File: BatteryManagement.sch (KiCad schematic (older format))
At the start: 0 parts

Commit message: Starting battery protection & management.
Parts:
- added U?: AP9211, symbol dingo-hat:AP9211
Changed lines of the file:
@@
 $Descr A4 11693 8268
 encoding utf-8
-Sheet 1 3
+Sheet 3 3
 Title ""
 Date ""
@@
 Comment4 ""
 $EndDescr
+$Comp
+L dingo-hat:AP9211 U?
+U 1 1 5DC173E3
+P 4400 3500
+F 0 "U?" H 4400 3925 50  0000 C CNN
+F 1 "AP9211" H 4400 3834 50  0000 C CNN
+F 2 "" H 4400 3350 50  0001 C CNN
+F 3 "https://www.diodes.com/assets/Datasheets/AP9211.pdf" H 4400 3350 50  0001 C CNN
+	1    4400 3500
+	1    0    0    -1
+$EndComp
 $EndSCHEMATC

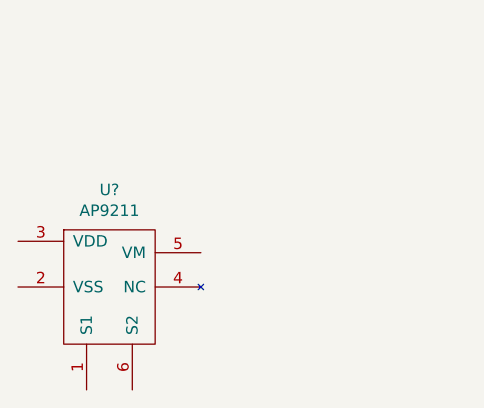
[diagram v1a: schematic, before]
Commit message: Changing structure, RM old power circuitry.
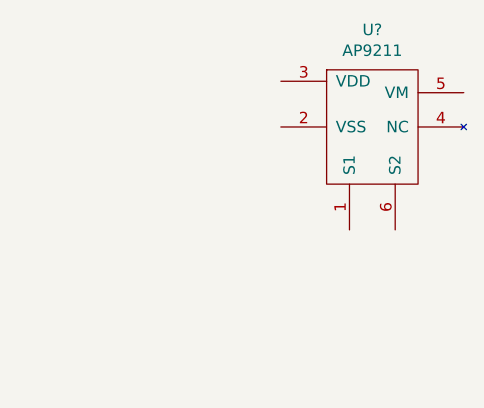
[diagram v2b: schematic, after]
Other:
- moved on the sheet: U?
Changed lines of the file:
@@
 L dingo-hat:AP9211 U?
 U 1 1 5DC173E3
-P 4400 3500
-F 0 "U?" H 4400 3925 50  0000 C CNN
-F 1 "AP9211" H 4400 3834 50  0000 C CNN
-F 2 "" H 4400 3350 50  0001 C CNN
-F 3 "https://www.diodes.com/assets/Datasheets/AP9211.pdf" H 4400 3350 50  0001 C CNN
-	1    4400 3500
+P 5550 2800
+AR Path="/5DA95EB0/5DAAD200/5DC173E3" Ref="U?"  Part="1"
+AR Path="/5DC297AB/5DC173E3" Ref="U?"  Part="1"
+F 0 "U?" H 5550 3225 50  0000 C CNN
+F 1 "AP9211" H 5550 3134 50  0000 C CNN
+F 2 "" H 5550 2650 50  0001 C CNN
+F 3 "https://www.diodes.com/assets/Datasheets/AP9211.pdf" H 5550 2650 50  0001 C CNN
+	1    5550 2800
 	1    0    0    -1
 $EndComp

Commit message: Battery work, need to get on to connectors.
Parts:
- added C401: 100nF, Capacitors_SMD:C_0603, symbol Device:C
- added J401: Bootstrap, Pin_Headers:Pin_Header_Straight_1x02_Pitch2.54mm, symbol Connector_Generic:Conn_01x02
- added R401: 470, Resistor_SMD:R_0603_1608Metric_Pad1.05x0.95mm_HandSolder, symbol Device:R
- added R402: 2k7, Resistor_SMD:R_0603_1608Metric_Pad1.05x0.95mm_HandSolder, symbol Device:R
- gave numbers to parts that had none: 1
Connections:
- net Batt-: now reaches U401.1 (S1)
- net Batt-: now also U401.2 (VSS), C401.2, J401.2 (Pin_2)
- net at U401.3 (VDD): now also C401.1, R401.2
- net BATT_S1: now reaches U401.5 (VM)
- net BATT_S1: now also R402.1
- net Pack-: now reaches U401.6 (S2)
- net Pack-: now also J401.1 (Pin_1), R402.2
- new net Batt+: R401.1
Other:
- note added: "Not sure if we'll need this to bring battery up on connect. Just do TH to check."
- moved on the sheet: U401
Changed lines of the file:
@@
 L dingo-hat:AP9211 U?
 U 1 1 5DC173E3
-P 5550 2800
+P 5550 3000
 AR Path="/5DA95EB0/5DAAD200/5DC173E3" Ref="U?"  Part="1"
-AR Path="/5DC297AB/5DC173E3" Ref="U?"  Part="1"
-F 0 "U?" H 5550 3225 50  0000 C CNN
-F 1 "AP9211" H 5550 3134 50  0000 C CNN
-F 2 "" H 5550 2650 50  0001 C CNN
-F 3 "https://www.diodes.com/assets/Datasheets/AP9211.pdf" H 5550 2650 50  0001 C CNN
-	1    5550 2800
+AR Path="/5DC297AB/5DC173E3" Ref="U401"  Part="1"
+F 0 "U401" H 5550 3425 50  0000 C CNN
+F 1 "AP9211" H 5550 3334 50  0000 C CNN
+F 2 "" H 5550 2850 50  0001 C CNN
+F 3 "https://www.diodes.com/assets/Datasheets/AP9211.pdf" H 5550 2850 50  0001 C CNN
+	1    5550 3000
 	1    0    0    -1
 $EndComp
+$Comp
+L Device:C C?
+U 1 1 5DD0667E
+P 4700 3050
+AR Path="/5DD0667E" Ref="C?"  Part="1"
+AR Path="/5DA95EB0/5DD0667E" Ref="C?"  Part="1"
+AR Path="/5DC297AB/5DD0667E" Ref="C401"  Part="1"
+F 0 "C401" H 4815 3096 50  0000 L CNN
+F 1 "100nF" H 4815 3005 50  0000 L CNN
+F 2 "Capacitors_SMD:C_0603" H 4738 2900 50  0001 C CNN
+F 3 "~" H 4700 3050 50  0001 C CNN
+F 4 "0603" H 4600 3150 50  0000 L TNN "Package"
+F 5 "CAP CER 0.1UF 50V X7R 0603" H 4700 3050 50  0001 C CNN "Description"
+F 6 "50V" H 4700 3000 50  0000 R TNN "Voltage Rating"
+F 7 "https://www.digikey.com/product-detail/en/samsung-electro-mechanics/CL10B104KB8NNNC/1276-1000-1-ND/3889086" H 4700 3050 50  0001 C CNN "Link"
+F 8 "Digi-Key" H 4700 3050 50  0001 C CNN "Supplier 1"
+F 9 "1276-1000-1-ND" H 4700 3050 50  0001 C CNN "Supplier Part Number 1"
+F 10 "0.15000" H 4700 3050 50  0001 C CNN "Unit Cost A$"
+	1    4700 3050
+	1    0    0    -1
+$EndComp
+$Comp
+L Device:R R?
+U 1 1 5DE42ED8
+P 6450 3150
+AR Path="/5DE42ED8" Ref="R?"  Part="1"
+AR Path="/5DC297AB/5DE42ED8" Ref="R402"  Part="1"
+F 0 "R402" V 6350 3050 50  0000 C CNN
+F 1 "2k7" V 6350 3250 50  0000 C CNN
+F 2 "Resistor_SMD:R_0603_1608Metric_Pad1.05x0.95mm_HandSolder" V 6380 3150 50  0001 C CNN
+F 3 "~" H 6450 3150 50  0001 C CNN
+F 4 "0603" H 5150 -2900 50  0001 C CNN "Package"
+	1    6450 3150
+	1    0    0    -1
+$EndComp
+Wire Wire Line
+	7450 3550 6450 3550
+Wire Wire Line
+	6450 3000 6450 2850
+Wire Wire Line
+	6450 2850 5950 2850
+Wire Wire Line
+	4700 2200 4700 2400
+Wire Wire Line
+	4700 2700 4700 2800
+Wire Wire Line
+	5450 3450 5450 3550
+Wire Wire Line
+	5450 3550 5100 3550
+Wire Wire Line
+	4700 3550 4700 3200
+Wire Wire Line
+	4700 2900 4700 2800
+Connection ~ 4700 2800
+Wire Wire Line
+	5150 3000 5100 3000
+Wire Wire Line
+	5100 3000 5100 3550
+Wire Wire Line
+	4700 3550 5100 3550
+Connection ~ 5100 3550
+Wire Wire Line
+	4700 2800 5150 2800
+Wire Wire Line
+	5650 3450 5650 3550
+Wire Wire Line
+	5650 3550 6450 3550
+Connection ~ 6450 3550
+Wire Wire Line
+	6450 3550 6450 3300
+Text HLabel 4700 2200 0    50   UnSpc ~ 0
+Batt+
+Text HLabel 7450 3550 2    50   UnSpc ~ 0
+Pack-
+Text HLabel 4700 3550 0    50   UnSpc ~ 0
+Batt-
+Wire Wire Line
+	4700 2200 7450 2200
+Text HLabel 7450 2200 2    50   UnSpc ~ 0
+Batt+
+$Comp
+L Device:R R?
+U 1 1 5DE426CE
+P 4700 2550
+AR Path="/5DE426CE" Ref="R?"  Part="1"
+AR Path="/5DC297AB/5DE426CE" Ref="R401"  Part="1"
+F 0 "R401" V 4600 2450 50  0000 C CNN
+F 1 "470" V 4600 2650 50  0000 C CNN
+F 2 "Resistor_SMD:R_0603_1608Metric_Pad1.05x0.95mm_HandSolder" V 4630 2550 50  0001 C CNN
+F 3 "~" H 4700 2550 50  0001 C CNN
+F 4 "0603" H 3400 -3500 50  0001 C CNN "Package"
+	1    4700 2550
+	1    0    0    -1
+$EndComp
+$Comp
+L Connector_Generic:Conn_01x02 J401
+U 1 1 5DE79FB0
+P 5600 3850
+F 0 "J401" V 5472 3930 50  0000 L CNN
+F 1 "Bootstrap" V 5563 3930 50  0000 L CNN
+F 2 "Pin_Headers:Pin_Header_Straight_1x02_Pitch2.54mm" H 5600 3850 50  0001 C CNN
+F 3 "~" H 5600 3850 50  0001 C CNN
+	1    5600 3850
+	0    1    1    0
+$EndComp
+Text Notes 5400 4000 0    50   ~ 0
+Not sure if we'll need this to bring battery up on connect. Just do TH to check.
+Wire Wire Line
+	5500 3650 5500 3550
+Wire Wire Line
+	5500 3550 5450 3550
+Connection ~ 5450 3550
+Wire Wire Line
+	5650 3550 5600 3550
+Wire Wire Line
+	5600 3550 5600 3650
+Connection ~ 5650 3550
+Text Label 6450 2850 0    50   ~ 0
+BATT_S1
 $EndSCHEMATC

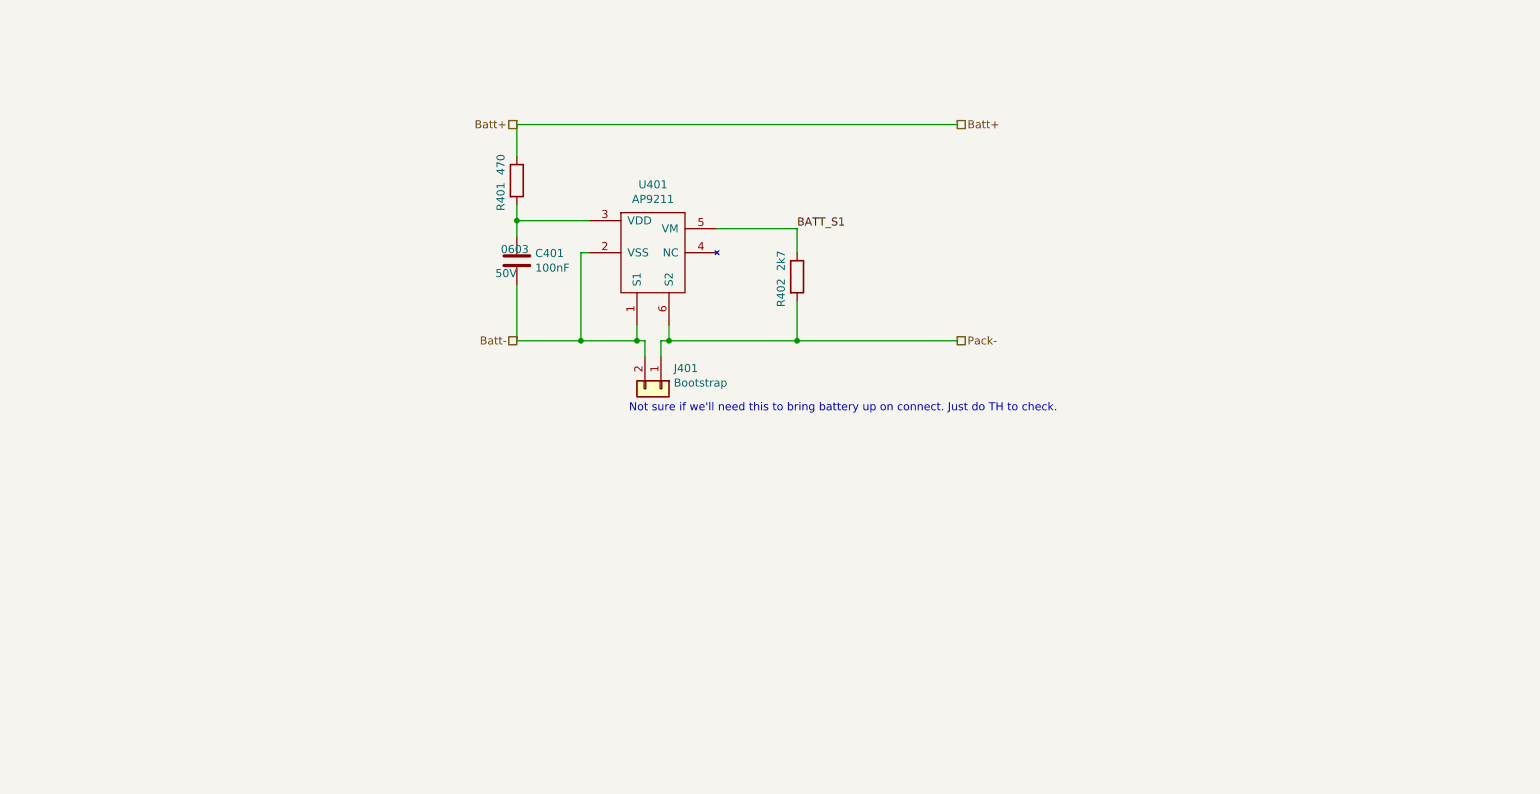
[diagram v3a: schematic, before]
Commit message: Charging. Do balance next if including.
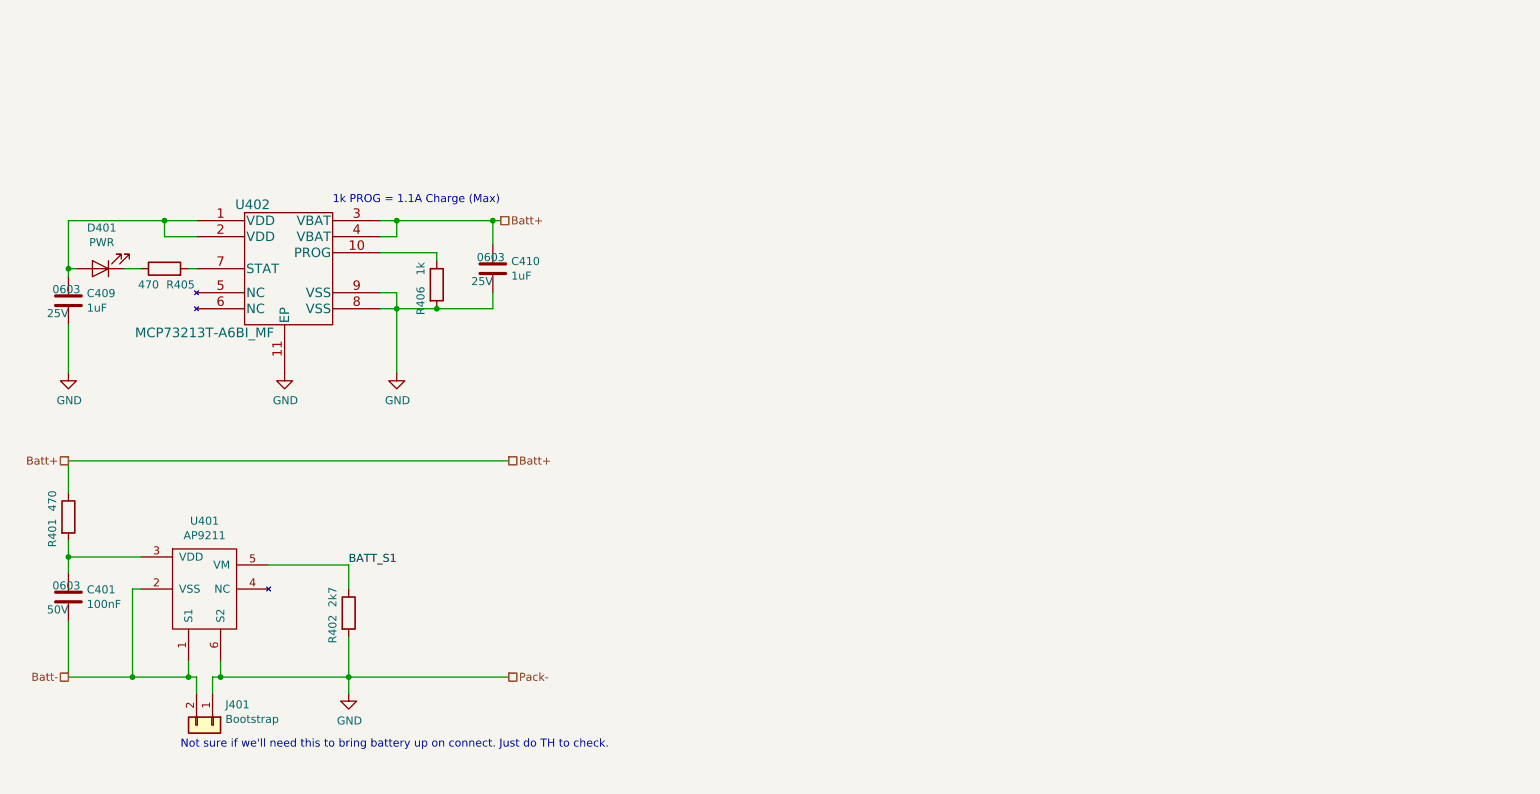
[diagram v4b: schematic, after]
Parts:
- added C409, C410: 1uF, Capacitors_SMD:C_0603, symbol Device:C
- added D401: PWR, LED_SMD:LED_0603_1608Metric_Pad1.05x0.95mm_HandSolder, symbol Device:LED
- added R405: 470, Resistor_SMD:R_0603_1608Metric_Pad1.05x0.95mm_HandSolder, symbol Device:R
- added R406: 1k, Resistor_SMD:R_0603_1608Metric_Pad1.05x0.95mm_HandSolder, symbol Device:R
- added U402: MCP73213T-A6BI_MF, libs:MCP73213T-A6BI, symbol dingo-hat:MCP73213T-A6BI_MF
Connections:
- net Batt+: now also C410.1, U402.3 (VBAT), U402.4 (VBAT)
- net Pack- renamed GND
- net GND: now also C409.2, C410.2, R406.2, U402.11 (EP), U402.8 (VSS), U402.9 (VSS)
- new net: C409.1, D401.2 (A), U402.1 (VDD), U402.2 (VDD)
- new net: R406.1, U402.10 (PROG)
- new net: R405.2, U402.7 (STAT)
- new net: D401.1 (K), R405.1
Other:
- note added: "1k PROG = 1.1A Charge (Max)"
- moved on the sheet: C401, J401, R401, R402, U401

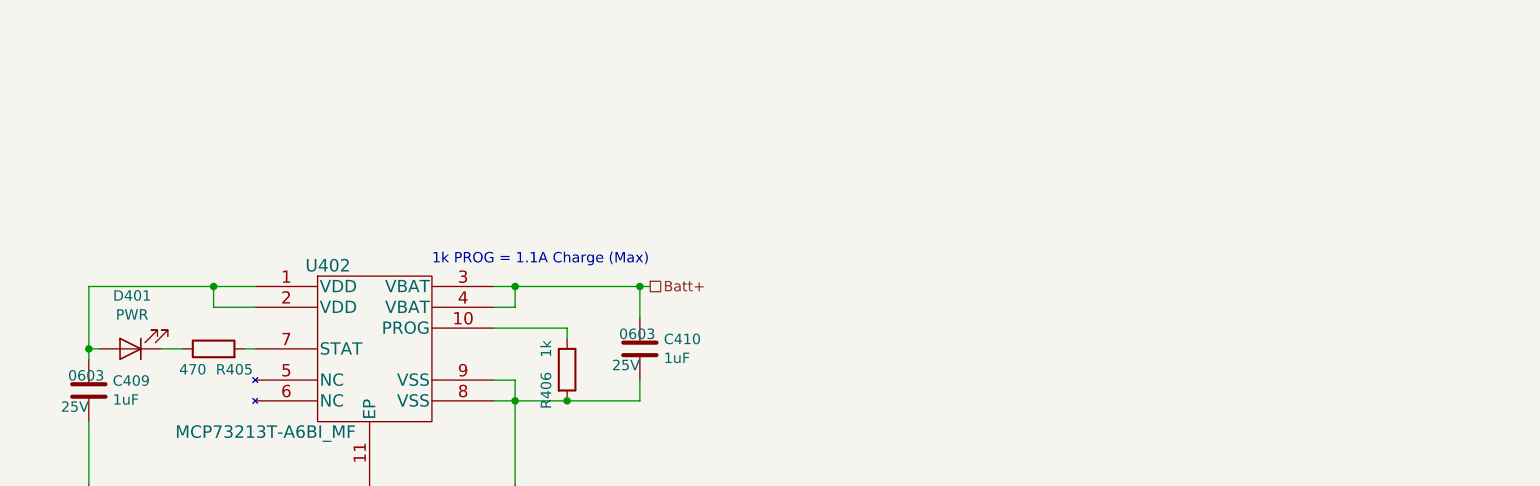
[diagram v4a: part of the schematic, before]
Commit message: Balance IC lib & footprint.
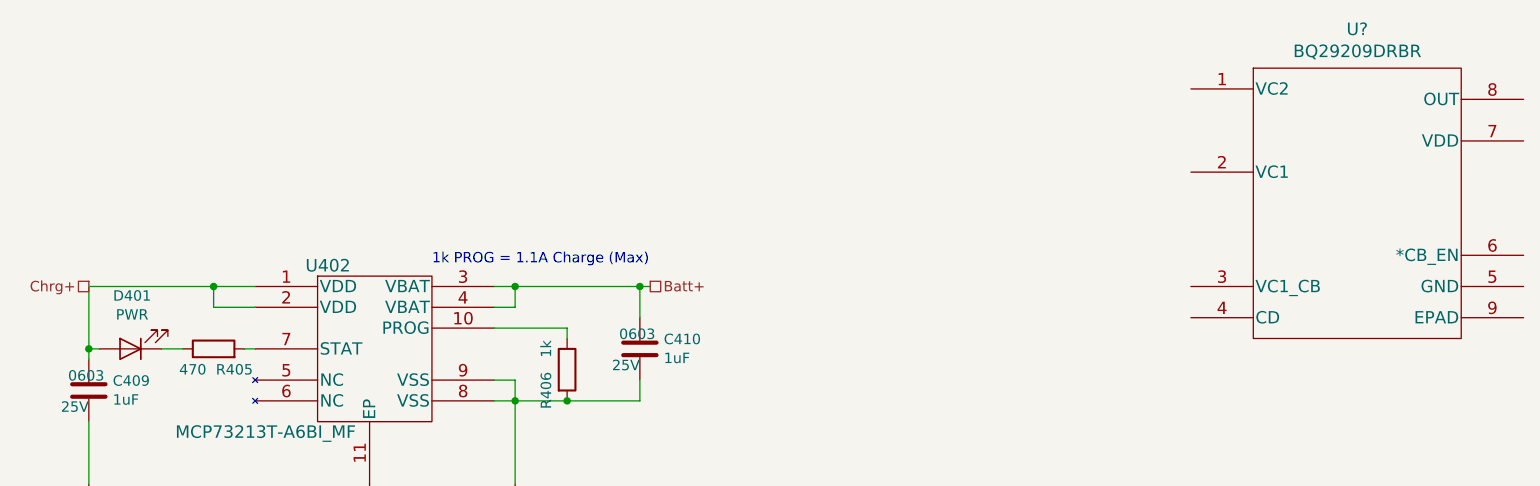
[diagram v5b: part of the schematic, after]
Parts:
- added U?: BQ29209DRBR, libs:BQ29209DRBR, symbol dingo-hat:BQ29209DRBR
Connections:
- net Chrg+: now reaches C409.1, D401.2 (A), U402.1 (VDD), U402.2 (VDD)
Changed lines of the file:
@@
 Text Notes 3550 2700 0    50   ~ 0
 1k PROG = 1.1A Charge (Max)
+Text HLabel 1900 2800 0    50   UnSpc ~ 0
+Chrg+
+$Comp
+L dingo-hat:BQ29209DRBR U?
+U 1 1 5DEB57B3
+P 8000 2400
+F 0 "U?" H 8000 3237 60  0000 C CNN
+F 1 "BQ29209DRBR" H 8000 3131 60  0000 C CNN
+F 2 "libs:BQ29209DRBR" H 8000 2400 60  0001 C CNN
+F 3 "" H 7200 2800 60  0000 C CNN
+	1    8000 2400
+	1    0    0    -1
+$EndComp
 $EndSCHEMATC
